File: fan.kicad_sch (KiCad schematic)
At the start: 14 parts, among them J6 Conn_01x04, U10 EMC2101

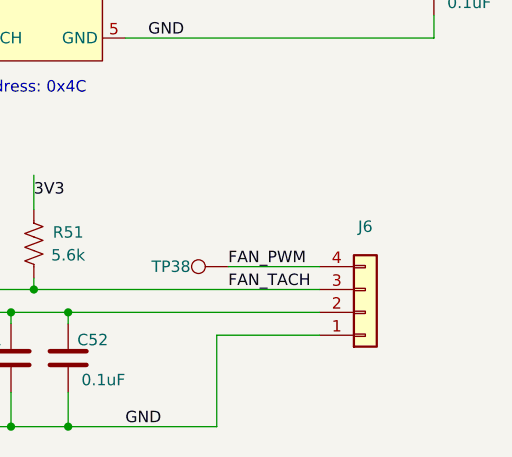
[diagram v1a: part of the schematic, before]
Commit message: JST fan connector
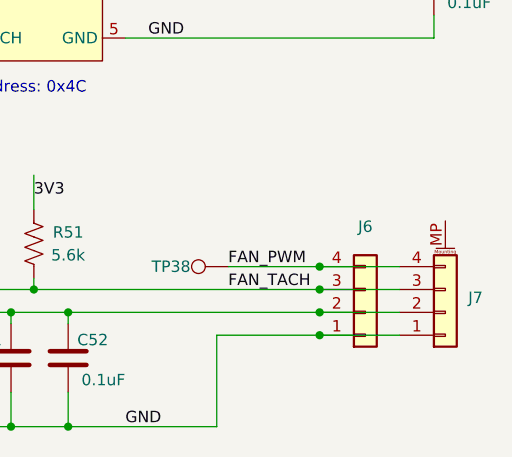
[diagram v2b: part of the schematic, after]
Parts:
- added J7: Conn_01x04, Connector_JST:JST_SH_BM04B-SRSS-TB_1x04-1MP_P1.00mm_Vertical, symbol Connector_Generic_MountingPin:Conn_01x04_MountingPin
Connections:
- net 5V: now also J7.2 (Pin_2)
- net FAN_PWM: now also J7.4 (Pin_4)
- net FAN_TACH: now also J7.3 (Pin_3)
- net GND: now also J7.1 (Pin_1)
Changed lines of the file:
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@@
+	)
+	(junction
+		(at 179.07 114.3)
+		(diameter 0)
+		(color 0 0 0 0)
 	)
 	(junction
@@
 	)
 	(junction
+		(at 179.07 111.76)
+		(diameter 0)
+		(color 0 0 0 0)
+	)
+	(junction
 		(at 106.68 86.36)
 		(diameter 0)
@@
 	)
 	(junction
+		(at 179.07 109.22)
+		(diameter 0)
+		(color 0 0 0 0)
+	)
+	(junction
 		(at 144.78 114.3)
+		(diameter 0)
+		(color 0 0 0 0)
+	)
+	(junction
+		(at 179.07 116.84)
 		(diameter 0)
 		(color 0 0 0 0)
@@
 	(wire
 		(pts
+			(xy 179.07 111.76) (xy 187.96 111.76)
+		)
+		(stroke
+			(width 0)
+			(type default)
+		)
+	)
+	(wire
+		(pts
+			(xy 151.13 127) (xy 167.64 127)
+		)
+		(stroke
+			(width 0)
+			(type default)
+		)
+	)
+	(wire
+		(pts
 			(xy 135.89 111.76) (xy 147.32 111.76)
 		)
@@
 	(wire
 		(pts
+			(xy 179.07 116.84) (xy 187.96 116.84)
+		)
+		(stroke
+			(width 0)
+			(type default)
+		)
+	)
+	(wire
+		(pts
 			(xy 179.07 66.04) (xy 191.77 66.04)
 		)
@@
 	(wire
 		(pts
+			(xy 167.64 116.84) (xy 167.64 127)
+		)
+		(stroke
+			(width 0)
+			(type default)
+		)
+	)
+	(wire
+		(pts
+			(xy 168.91 109.22) (xy 179.07 109.22)
+		)
+		(stroke
+			(width 0)
+			(type default)
+		)
+	)
+	(wire
+		(pts
 			(xy 120.65 83.82) (xy 132.08 83.82)
 		)
@@
 	(wire
 		(pts
-			(xy 167.64 116.84) (xy 167.64 127)
-		)
-		(stroke
-			(width 0)
-			(type default)
-		)
-	)
-	(wire
-		(pts
 			(xy 191.77 81.28) (xy 191.77 83.82)
 		)
@@
 	(wire
 		(pts
-			(xy 168.91 109.22) (xy 179.07 109.22)
+			(xy 179.07 114.3) (xy 187.96 114.3)
 		)
 		(stroke
@@
 	(wire
 		(pts
+			(xy 179.07 109.22) (xy 187.96 109.22)
+		)
+		(stroke
+			(width 0)
+			(type default)
+		)
+	)
+	(wire
+		(pts
 			(xy 144.78 114.3) (xy 144.78 115.57)
-		)
-		(stroke
-			(width 0)
-			(type default)
-		)
-	)
-	(wire
-		(pts
-			(xy 151.13 127) (xy 167.64 127)
 		)
 		(stroke
@@
 					(unit 1)
 				)
+			)
+		)
+	)
+	(symbol
+		(lib_id "Connector_Generic_MountingPin:Conn_01x04_MountingPin")
+		(at 193.04 114.3 0)
+		(mirror x)
+		(unit 1)
+		(exclude_from_sim no)
+		(in_bom yes)
+		(on_board yes)
+		(dnp no)
+		(fields_autoplaced yes)
+		(property "Reference" "J7"
+			(at 195.58 112.6743 0)
+			(effects
+				(font
+					(size 1.27 1.27)
+				)
+				(justify left)
+			)
+		)
+		(property "Value" "Conn_01x04"
+			(at 193.04 104.775 0)
+			(effects
+				(font
+					(size 1.27 1.27)
+				)
+				(hide yes)
+			)
+		)
+		(property "Footprint" "Connector_JST:JST_SH_BM04B-SRSS-TB_1x04-1MP_P1.00mm_Vertical"
+			(at 193.04 114.3 0)
+			(effects
+				(font
+					(size 1.27 1.27)
+				)
+				(hide yes)
+			)
+		)
+		(property "Datasheet" "~"
+			(at 193.04 114.3 0)
+			(effects
+				(font
+					(size 1.27 1.27)
+				)
+				(hide yes)
+			)
+		)
+		(property "Description" "Generic connectable mounting pin connector, single row, 01x04, script generated (kicad-library-utils/schlib/autogen/connector/)"
+			(at 193.04 114.3 0)
+			(effects
+				(font
+					(size 1.27 1.27)
+				)
+				(hide yes)
+			)
+		)
+		(property "PARTNO" ""
+			(at 193.04 114.3 0)
+			(effects
+				(font
+					(size 1.27 1.27)
+				)
+				(hide yes)
+			)
+		)
+		(property "DK" ""
+			(at 193.04 114.3 0)
+			(effects
+				(font
+					(size 1.27 1.27)
+				)
+				(hide yes)
+			)
+		)
+		(pin "1"
+		)
+		(pin "2"
+		)
+		(pin "3"
+		)
+		(pin "4"
+		)
+		(pin "MP"
+		)
+		(instances
+			(project "bitaxeGamma"
+				(path "/e63e39d7-6ac0-4ffd-8aa3-1841a4541b55/8e8832ea-6bf1-49d2-b3a5-32a207f555d2"
+					(reference "J7")
+					(unit 1)
+				)
